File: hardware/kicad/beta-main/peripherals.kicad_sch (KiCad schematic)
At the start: 23 parts, among them J10 Servo Socket, J11 Servo Socket, J12 Servo Socket, J13 Servo Socket, J14 Conn_01x04_Pin, J15 Conn_01x04_Pin, J16 Conn_01x04_Pin, J17 Conn_01x04_Pin, J19 FAN0, J20 FAN1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

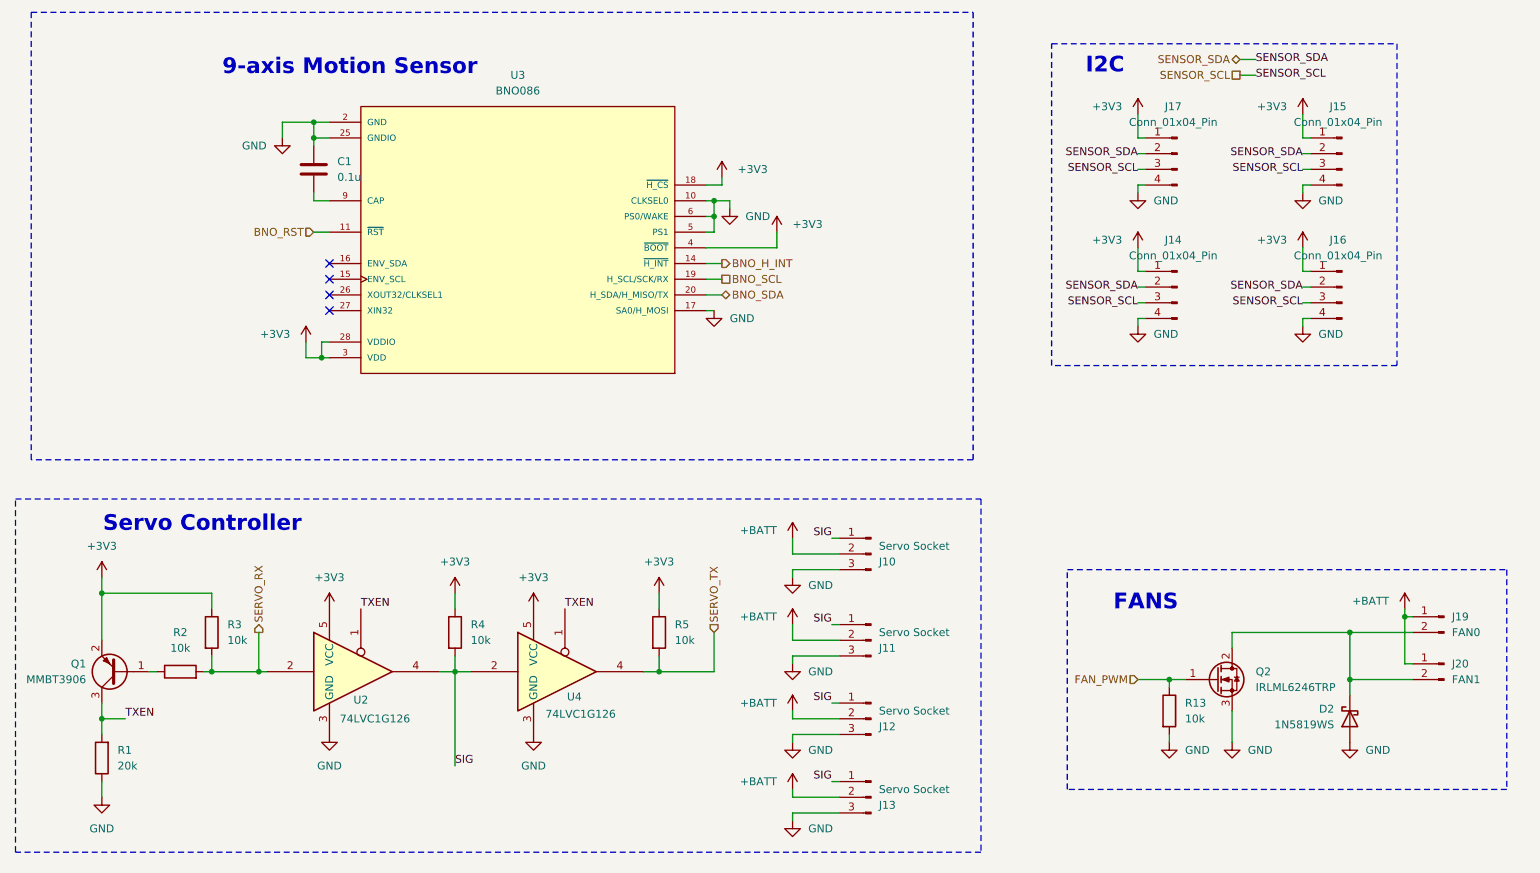
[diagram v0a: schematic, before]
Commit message: BOM, all easily found parts from digi
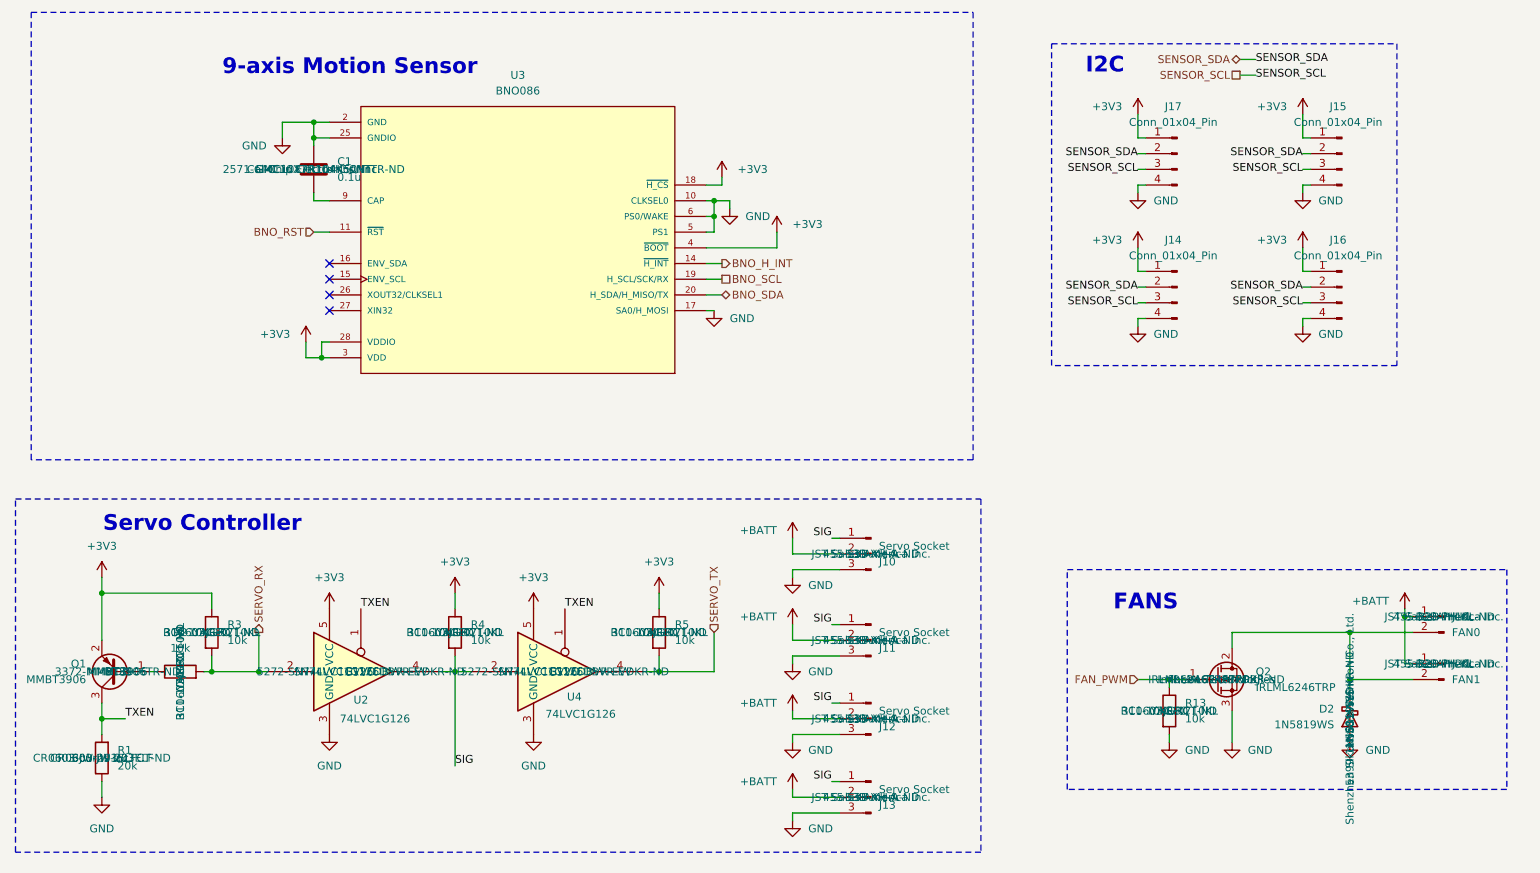
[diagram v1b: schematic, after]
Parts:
- C1: DigiKey_Part_Number (none) -> 2571-GMC10X7R104K50NTTR-ND; MANUFACTURER (none) -> Cal-Chip Electronics, Inc.; MP (none) -> GMC10X7R104K50NT
- D2: DigiKey_Part_Number (none) -> 5399-1N5819WSDKR-ND; MANUFACTURER (none) -> Shenzhen Slkormicro Semicon Co., Ltd.; MP (none) -> 1N5819WS
- J10, J11, J12, J13: DigiKey_Part_Number (none) -> 455-S3B-XH-A-ND; MANUFACTURER (none) -> JST Sales America Inc.; MP (none) -> S3B-XH-A
- J19, J20: DigiKey_Part_Number (none) -> 455-B2B-PH-KL-ND; MANUFACTURER (none) -> JST Sales America Inc.; MP (none) -> B2B-PH-KL
- Q1: DigiKey_Part_Number (none) -> 3372-MMBT3906TR-ND; MANUFACTURER (none) -> MDD; MP (none) -> MMBT3906
- Q2: DigiKey_Part_Number (none) -> IRLML6246TRPBFDKR-ND; MANUFACTURER (none) -> Infineon Technologies; MP (none) -> IRLML6246TRPBF
- R1: DigiKey_Part_Number (none) -> CR0603-JW-203ELFCT-ND; MANUFACTURER (none) -> Bourns Inc.; MP (none) -> CR0603-JW-203ELF
- R13, R2, R3, R4, R5: DigiKey_Part_Number (none) -> 311-10KGRCT-ND; MANUFACTURER (none) -> YAGEO; MP (none) -> RC0603JR-0710KL
- U2, U4: DigiKey_Part_Number (none) -> 5272-SN74LVC1G126DBVR-EVDKR-ND; MANUFACTURER (none) -> EVVO; MP (none) -> SN74LVC1G126DBVR-EV
